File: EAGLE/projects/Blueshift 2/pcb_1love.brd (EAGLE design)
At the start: 96.5 x 226.1 mm, 20 parts, among them X1 RASPI_BOARD_B+_F

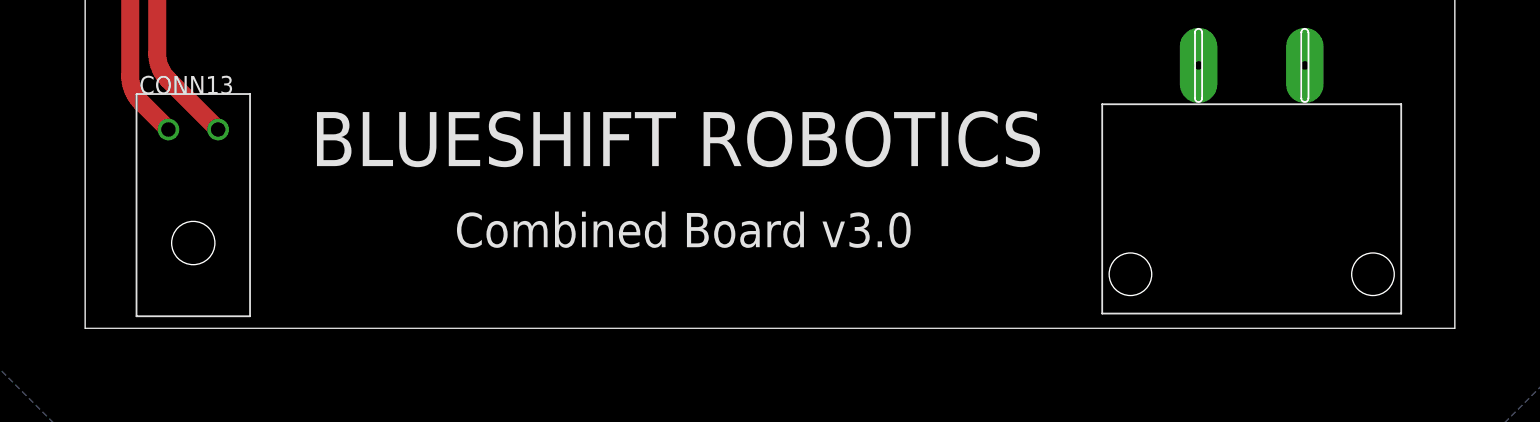
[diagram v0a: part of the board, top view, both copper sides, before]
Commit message: fixed hole in pcb
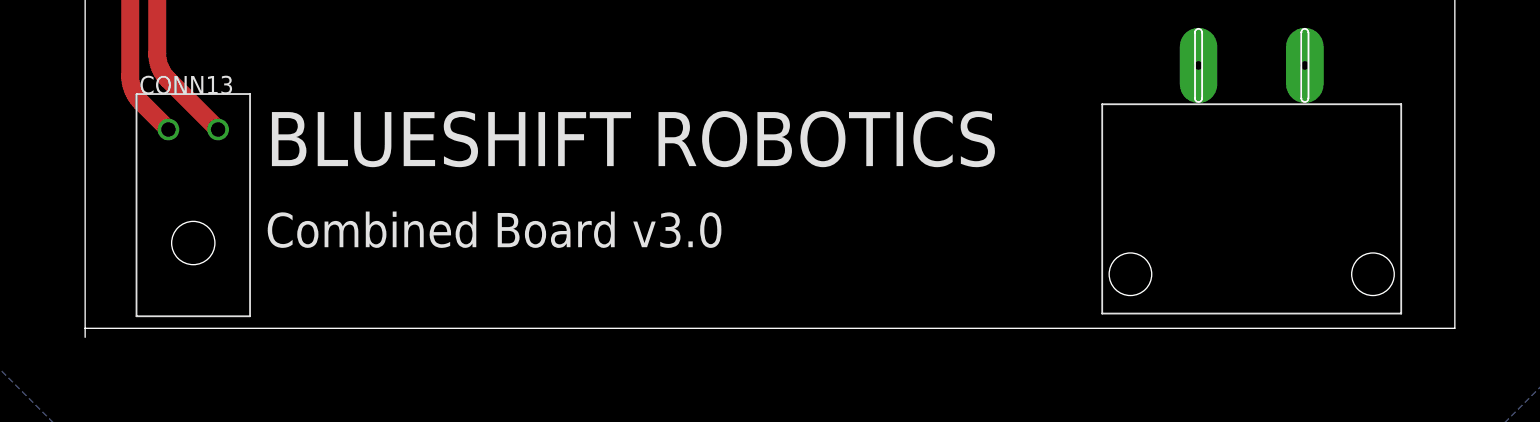
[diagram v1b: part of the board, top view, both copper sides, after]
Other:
- board size 96.5 x 226.1 mm -> 96.5 x 226.7 mm
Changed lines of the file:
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@@
 <?xml version="1.0" encoding="utf-8"?>
 <!DOCTYPE eagle SYSTEM "eagle.dtd">
-<eagle version="9.6.0">
+<eagle version="9.6.1">
 <drawing>
 <settings>
@@
 <board>
 <plain>
-<wire x1="0" y1="0" x2="96.52" y2="0" width="0" layer="21"/>
 <wire x1="96.52" y1="0" x2="96.52" y2="164.465" width="0" layer="20"/>
 <wire x1="96.52" y1="164.465" x2="86.995" y2="164.465" width="0" layer="20"/>
@@
 <wire x1="55.88" y1="203.835" x2="0" y2="203.835" width="0" layer="20"/>
 <wire x1="0" y1="203.835" x2="0" y2="0" width="0" layer="20"/>
-<text x="15.875" y="11.43" size="3.81" layer="21">BLUESHIFT ROBOTICS</text>
-<text x="26.035" y="5.715" size="2.413" layer="21">Combined Board v3.0</text>
+<text x="12.7" y="11.43" size="3.81" layer="21">BLUESHIFT ROBOTICS</text>
+<text x="12.7" y="5.715" size="2.413" layer="21">Combined Board v3.0</text>
+<wire x1="0" y1="0" x2="0" y2="-0.635" width="0" layer="20"/>
+<wire x1="0" y1="0" x2="96.52" y2="0" width="0" layer="20"/>
 </plain>
 <attributes>
